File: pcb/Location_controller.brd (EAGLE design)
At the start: 75 x 48 mm, 50 parts, among them IC1 LIS302DL

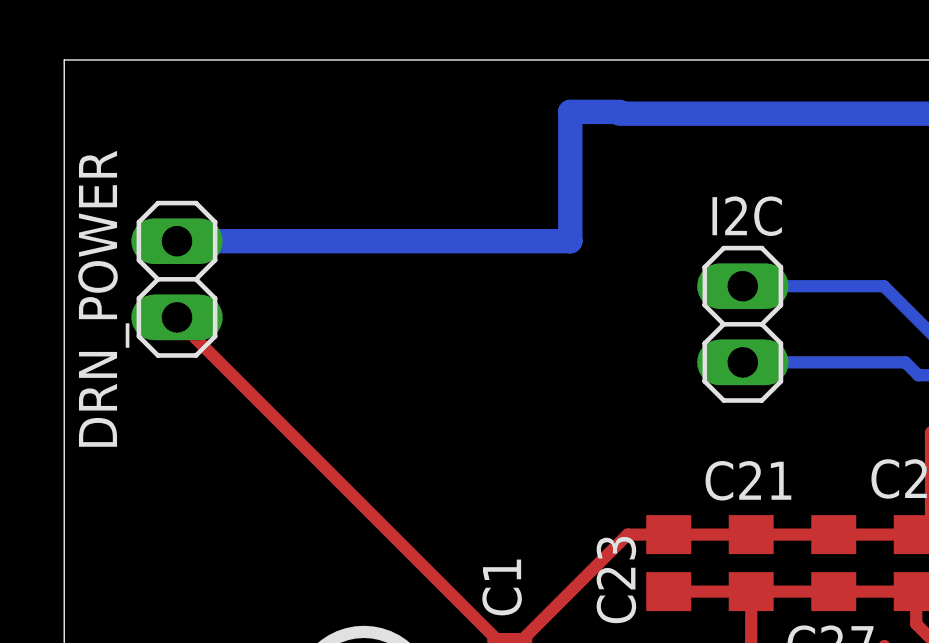
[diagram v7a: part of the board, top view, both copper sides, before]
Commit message: Add Zener Diodes to I2C pins
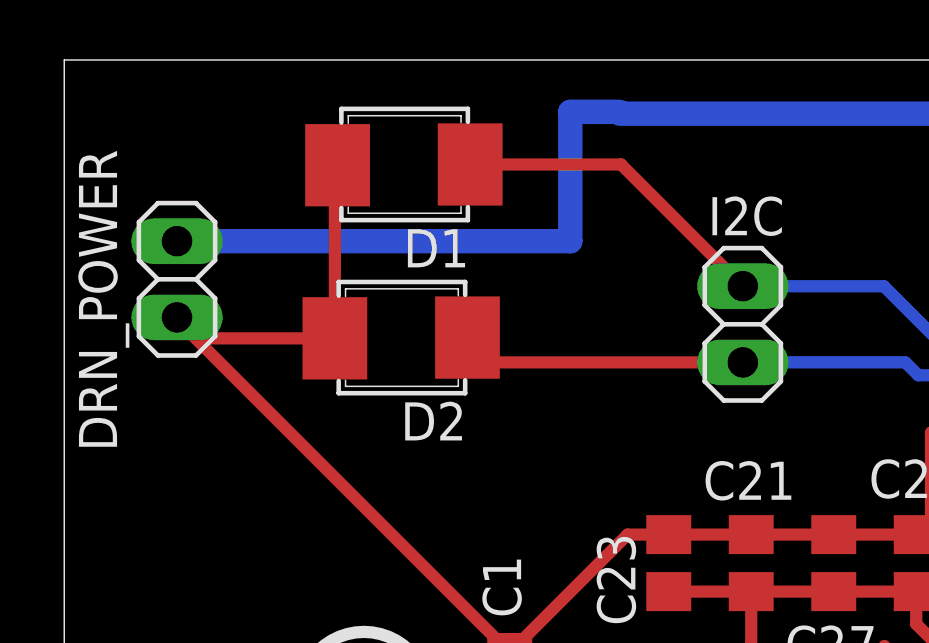
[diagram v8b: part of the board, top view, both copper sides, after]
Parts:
- added D1, D2: ZDIODE, stm32f4:SMB
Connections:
- net GND: now also D1.2, D2.2
- net I2C_SCL: now also D2.1
- net I2C_SDA: now also D1.1
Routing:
- net GND: track 346.7 -> 358.1 mm
- net I2C_SDA: track 27.8 -> 38.6 mm
- net I2C_SCL: track 27.4 -> 36.9 mm
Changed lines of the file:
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@@
 <attribute name="VALUE" x="19.445" y="41.73" size="1.27" layer="27" rot="R270"/>
 </element>
+<element name="D1" library="stm32f4" package="SMB" value="ZDIODE" x="11.22" y="44.39" rot="R180"/>
+<element name="D2" library="stm32f4" package="SMB" value="ZDIODE" x="11.13" y="38.62" rot="R180"/>
 </elements>
 <signals>
@@
 <wire x1="58.75" y1="9.36" x2="59.53" y2="8.58" width="0.4064" layer="1"/>
 <wire x1="59.53" y1="8.58" x2="70.71" y2="8.58" width="0.4064" layer="1"/>
+<contactref element="D1" pad="2"/>
+<contactref element="D2" pad="2"/>
+<wire x1="9.1118" y1="44.4916" x2="9.0218" y2="44.4916" width="0.4064" layer="1"/>
+<wire x1="9.0218" y1="44.4916" x2="9.0218" y2="38.7216" width="0.4064" layer="1"/>
+<wire x1="9.0218" y1="38.7216" x2="4.4584" y2="38.7216" width="0.4064" layer="1"/>
+<wire x1="4.4584" y1="38.7216" x2="3.76" y2="39.42" width="0.4064" layer="1"/>
 </signal>
 <signal name="N$1">
@@
 <via x="39.08" y="35.47" extent="1-16" drill="0.6" shape="square"/>
 <wire x1="39.08" y1="35.47" x2="39.08" y2="35.18" width="0.4064" layer="1"/>
+<contactref element="D2" pad="1"/>
+<wire x1="13.4414" y1="38.747" x2="14.2684" y2="37.92" width="0.4064" layer="1"/>
+<wire x1="14.2684" y1="37.92" x2="22.62" y2="37.92" width="0.4064" layer="1"/>
 </signal>
 <signal name="I2C_SDA">
@@
 <wire x1="29.15" y1="38.63" x2="35.52" y2="38.63" width="0.4064" layer="16"/>
 <wire x1="35.52" y1="38.63" x2="35.77" y2="38.88" width="0.4064" layer="16"/>
+<contactref element="D1" pad="1"/>
+<wire x1="13.5314" y1="44.517" x2="18.563" y2="44.517" width="0.4064" layer="1"/>
+<wire x1="18.563" y1="44.517" x2="22.62" y2="40.46" width="0.4064" layer="1"/>
 </signal>
 <signal name="N$8">
